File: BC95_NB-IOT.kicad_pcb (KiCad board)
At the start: 4 copper layers, 99.1 x 80 mm, 162 parts, among them J1 VIN, J2 SWD, J3 USB_B_Micro, J4 ANALOG_IN, J5 SIM_Card_Shielded, J6 INPUT, J7 OUTPUT, J8 EMPTY_PIN, Q1 2N7002, Q10 Si2301CDS, Q11 2N7002, Q12 2N7002, Q13 2N7002, Q2 2N7002, Q3 Si2301CDS, Q4 2N7002, Q5 2N7002, Q6 Si2301CDS, Q7 2N7002, Q8 2N7002, Q9 2N7002, SW1 RESET, U1 SHT4x, U10 FAN2558SX, U2 TPS54331DDA, U3 STM32L051K6Tx, U4 BG96, U5 TXS0108EPW, U6 TLV704xx, U7 FOD817ASD, U8 FOD817ASD, U9 LM1085-ADJ

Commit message: placement and routing
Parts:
- removed R64: 10k, Resistor_SMD:R_0603_1608Metric
- added C48: 100nF, Capacitor_SMD:C_0603_1608Metric, F.Cu at (75.4, 57.1)
- added C49: 100nF, Capacitor_SMD:C_0603_1608Metric, F.Cu at (70.9, 57.1)
- added D10: SMAJ28CA, Diode_SMD:D_SMA, F.Cu at (50.8, 81.0)
- added D11: SMAJ28CA, Diode_SMD:D_SMA, F.Cu at (127.4, 50.5)
- added D12: SMAJ28CA, Diode_SMD:D_SMA, F.Cu at (122.5, 50.5)
- added D13: SMAJ28CA, Diode_SMD:D_SMA, F.Cu at (99.2, 50.9)
- added D14: SMAJ28CA, Diode_SMD:D_SMA, F.Cu at (94.4, 50.8)
- added D15: SMAJ28CA, Diode_SMD:D_SMA, F.Cu at (70.6, 50.8)
- added D16: SMAJ28CA, Diode_SMD:D_SMA, F.Cu at (66.0, 50.8)
- added D17: ESDA6V1-5SC6, Package_TO_SOT_SMD:SOT-23-6, F.Cu at (133.9, 63.6)
- added R66: 470, Resistor_SMD:R_0603_1608Metric, F.Cu at (98.3, 59.4)
- added REF**: OSHW-Logo2_7.3x6mm_SilkScreen, Symbol:OSHW-Logo2_7.3x6mm_SilkScreen, F.Cu at (134.9, 53.1)
- added REF**: KiCad-Logo2_5mm_SilkScreen, Symbol:KiCad-Logo2_5mm_SilkScreen, F.Cu at (133.3, 96.5)
- added REF**: ESD-Logo_13.2x12mm_SilkScreen, Symbol:ESD-Logo_13.2x12mm_SilkScreen, F.Cu at (67.3, 103.4)
- AE1, AE2: footprint Connector_Coaxial:SMA_Amphenol_901-143_Horizontal -> Connector_Coaxial:SMA_Amphenol_901-144_Vertical
- J5: footprint Connector_Card:microSIM_JAE_SF53S006VCBR2000 -> ATTEND_MICRO_SIM:ATTEND_MICRO_SIM
- moved C30 185.6 mm to (-40.9, 56.6)
- moved D7 185.6 mm to (-28.9, 54.6)
- moved D8 185.6 mm to (-25.2, 50.2)
- moved D9 185.6 mm to (-20.9, 47.3)
- moved Q12 185.6 mm to (20.3, 8.07)
- moved Q4 185.6 mm to (-7.14, 33.1)
- moved Q8 185.6 mm to (2.90, 26.7)
- moved R12 185.6 mm to (9.86, 16.0)
- moved R30 185.6 mm to (-44.9, 56.6)
- moved R33 185.6 mm to (-33.1, 44.5)
- moved R34 185.6 mm to (15.9, 2.36)
- moved R37 185.6 mm to (26.7, -3.93)
- moved R42 185.6 mm to (0.17, 20.7)
- moved R45 185.6 mm to (-2.17, 18.2)
- moved R46 185.6 mm to (7.80, 5.96)
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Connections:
- net Net-(R10-Pad2) renamed ANALOG_IN1
- net Net-(R15-Pad1) renamed ANALOG_IN2
- D2 pad 5: unconnected-(D2-Pad5) -> +3V3
- D5 pad 5: /USB_D+ -> unconnected-(D5-Pad5)
- D5 pad 6: /USB_D- -> unconnected-(D5-Pad6)
- Q13 pad 1: 1.8V_EN -> Net-(Q13-Pad1)
- R59 pad 1: 1.8V_EN -> Net-(Q13-Pad1)
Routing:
- net +24V: track 6.32 -> 130.0 mm, vias 26 -> 28
- net V_OUT1: track 0.00 -> 80.8 mm, vias 0 -> 2
- net +3V8: track 55.0 -> 112.0 mm, vias 11 -> 58
- net +3V3: track 62.8 -> 115.4 mm, vias 2 -> 5
- net V_OUT2: track 0.00 -> 48.2 mm, vias 0 -> 2
- net V_IN2: track 0.00 -> 45.8 mm, vias 0 -> 2
- net MODULE_UART_TX: track 0.00 -> 45.1 mm, vias 0 -> 2
- net 1.8V_MONITOR: track 0.00 -> 45.0 mm, vias 0 -> 3
- net SWCLK: track 23.3 -> 64.5 mm, vias 0 -> 2
- net Net-(J4-Pad1): track 0.00 -> 39.7 mm
- net MODULE_UART_RX: track 0.00 -> 39.1 mm, vias 0 -> 3
- net Net-(R18-Pad1): track 0.00 -> 36.4 mm, vias 0 -> 2
- net V_IN1: track 0.00 -> 35.1 mm, vias 0 -> 2
- net LLC_EN: track 0.00 -> 34.0 mm, vias 0 -> 2
- net /SIM_DATA: track 0.00 -> 32.5 mm, vias 0 -> 2
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- added copper zone on F.Cu, net +6V
- added copper zone on In2.Cu, net +6V
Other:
- board size 99.1 x 80 mm -> 118.3 x 80 mm

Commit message: routing
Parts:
- removed REF**: OSHW-Logo2_7.3x6mm_SilkScreen, Symbol:OSHW-Logo2_7.3x6mm_SilkScreen
- removed REF**: KiCad-Logo2_5mm_SilkScreen, Symbol:KiCad-Logo2_5mm_SilkScreen
- removed REF**: ESD-Logo_13.2x12mm_SilkScreen, Symbol:ESD-Logo_13.2x12mm_SilkScreen
- Q11, Q12, Q4, Q5, Q8, Q9: value 2N7002 -> FDV303N
- moved R30 178.6 mm to (130.8, 88.1), turned to 90 degrees
- moved R49 176.0 mm to (132.3, 98.3)
- moved R33 166.6 mm to (132.3, 63.6), turned to -90 degrees
- moved D8 166.0 mm to (135.6, 91.4)
- moved D9 164.7 mm to (135.6, 98.3)
- moved D7 163.9 mm to (134.6, 66.3)
- moved R44 153.7 mm to (132.6, 95.1), turned to -90 degrees
- moved Q9 152.1 mm to (135.3, 59.3), turned to 0 degrees
- moved R42 150.3 mm to (130.8, 95.0), turned to 90 degrees
- moved Q8 149.1 mm to (135.4, 95.0), turned to 0 degrees
- moved R13 149.0 mm to (119.2, 63.3), turned to 0 degrees
- moved R38 147.5 mm to (132.6, 91.4)
- moved Q4 145.8 mm to (135.4, 63.6), turned to 0 degrees
- moved R34 144.9 mm to (132.6, 88.1), turned to -90 degrees
- moved Q5 143.7 mm to (135.4, 88.1), turned to 0 degrees
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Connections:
- C35 pad 1: 1.8V_MONITOR -> +1V8
- C45 pad 1: 1.8V_MONITOR -> +1V8
- C46 pad 1: 1.8V_MONITOR -> +1V8
- R61 pad 1: 1.8V_MONITOR -> +1V8
- U10 pad 6: 1.8V_MONITOR -> +1V8
- U5 pad 2: 1.8V_MONITOR -> +1V8
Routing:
- net MODULE_RST: track 0.00 -> 77.1 mm, vias 0 -> 2
- net AIRPLANE_MODE: track 0.00 -> 74.3 mm, vias 0 -> 2
- net MODULE_ON: track 0.00 -> 52.3 mm, vias 0 -> 2
- net PWR_EN: track 2.14 -> 52.2 mm, vias 1 -> 3
- net +1V8: track 0.00 -> 46.9 mm, vias 0 -> 3
- net 1.8V_MONITOR: track 45.0 -> 0.00 mm, vias 3 -> 0
- net +3V8: track 112.0 -> 156.0 mm, vias 58 -> 66
- net RESET: track 0.00 -> 35.3 mm, vias 0 -> 2
- net STATUS: track 0.00 -> 34.1 mm, vias 0 -> 2
- net NETLIGHT: track 0.00 -> 33.0 mm, vias 0 -> 2
- net PSM_IND: track 0.00 -> 31.6 mm, vias 0 -> 2
- net MODULE_UART_RX: track 39.1 -> 62.0 mm, vias 3 -> 4
- net W_DISABLE: track 0.00 -> 22.6 mm
- net PWRKEY: track 0.00 -> 18.8 mm
- net MODULE_UART_TX: track 45.1 -> 63.2 mm, vias 2 -> 3
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
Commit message: routing
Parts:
- C20, C22, C23, C25, D5, J5, R11, R14, R17, R18, R65: moved to B.Cu
- moved J5 23.2 mm to (96.5, 88.1), turned to 180 degrees
- moved D5 23.0 mm to (73.1, 101.9), turned to 180 degrees
- moved C22 19.0 mm to (88.8, 89.4), turned to 90 degrees
- moved R65 16.3 mm to (73.1, 96.2)
- moved C25 16.0 mm to (73.1, 94.2), turned to 180 degrees
- moved C20 15.1 mm to (82.4, 89.5), turned to 90 degrees
- moved C23 14.6 mm to (85.5, 89.4), turned to 90 degrees
- moved R11 8.91 mm to (90.6, 89.4)
- moved R18 8.74 mm to (92.3, 89.4)
- moved Q12 6.25 mm to (97.6, 84.9), turned to 0 degrees
- moved R57 4.82 mm to (93.0, 84.8), turned to 90 degrees
- moved R58 4.27 mm to (94.7, 84.9), turned to -90 degrees
- moved R14 3.79 mm to (83.9, 89.6)
- moved AE2 2.80 mm to (103.1, 106.6)
- moved C4 2.80 mm to (106.3, 100.1)
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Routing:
- net GND: track 0.00 -> 112.2 mm, vias 0 -> 214
- net Net-(D2-Pad1): track 3.56 -> 35.0 mm, vias 0 -> 1
- net Net-(C25-Pad1): track 36.5 -> 59.4 mm, vias 2 -> 1
- net +3V3: track 117.1 -> 138.9 mm, vias 5 -> 6
- net /SIM_RST: track 32.2 -> 19.3 mm, vias 2 -> 0
- net MODULE_RST: track 77.1 -> 67.0 mm
- net Net-(D14-Pad2): track 17.3 -> 27.2 mm, vias 0 -> 1
- net Net-(R11-Pad2): track 25.7 -> 16.7 mm, vias 2 -> 1
- net /SIM_DATA: track 32.5 -> 27.3 mm
- net ANT_GNSS: track 16.8 -> 12.1 mm
- net Net-(R14-Pad2): track 19.6 -> 23.7 mm, vias 0 -> 1
- net +6V: track 43.8 -> 40.4 mm
- net RESET: track 35.3 -> 32.2 mm
- net /SIM_CLK: track 30.5 -> 28.5 mm
- net +24V: track 132.2 -> 130.3 mm
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- added copper zone on In1.Cu, net +24V
- added copper zone on In1.Cu, net +3V8
- added copper zone on In1.Cu, net +6V
- added copper zone on F.Cu, net GND
- added copper zone on In2.Cu, net GND
- added copper zone on In1.Cu, net Net-(C17-Pad2)
- added copper zone on In1.Cu, net Net-(C39-Pad1)
- added copper zone on In1.Cu, net Net-(D1-Pad2)
- added copper zone on In1.Cu, net Net-(D10-Pad2)
- removed copper zone on In2.Cu, net +24V
- removed copper zone on In2.Cu, net +3V8
- removed copper zone on In2.Cu, net +6V
- removed copper zone on In2.Cu, net Net-(C17-Pad2)
- removed copper zone on In2.Cu, net Net-(C39-Pad1)
- removed copper zone on In2.Cu, net Net-(D1-Pad2)
- removed copper zone on In2.Cu, net Net-(D10-Pad2)

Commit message: board layout
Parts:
- added R64: 10k, Resistor_SMD:R_0603_1608Metric, F.Cu at (77.1, 57.1)
- added REF**: hyc, HYC:hyc, F.Cu at (73.9, 67.7)
- U4: value BG96 -> QUECTEL_BG96
- moved C1 2.58 mm to (80.1, 71.0), turned to 180 degrees
- moved R50 2.04 mm to (66.3, 84.7)
- moved R52 1.78 mm to (64.5, 84.7)
- moved C48 0.15 mm to (75.3, 57.1)
- moved U4 0.06 mm to (115.0, 80.7)
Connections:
- U3 pad 9: 1.8V_MONITOR -> +1V8
- U4 pad 12: unconnected-(U4-Pad11) -> unconnected-(U4-Pad12)
- U4 pad 13: unconnected-(U4-Pad11) -> unconnected-(U4-Pad13)
- U4 pad 14: unconnected-(U4-Pad11) -> unconnected-(U4-Pad14)
- U4 pad 16: unconnected-(U4-Pad11) -> unconnected-(U4-Pad16)
- U4 pad 25: unconnected-(U4-Pad11) -> unconnected-(U4-Pad25)
- U4 pad 51: unconnected-(U4-Pad11) -> unconnected-(U4-Pad51)
- U4 pad 56: unconnected-(U4-Pad11) -> unconnected-(U4-Pad56)
- U4 pad 57: unconnected-(U4-Pad11) -> unconnected-(U4-Pad57)
- U4 pad 63: unconnected-(U4-Pad11) -> unconnected-(U4-Pad63)
- U4 pad 65: unconnected-(U4-Pad11) -> unconnected-(U4-Pad65)
- U4 pad 66: unconnected-(U4-Pad11) -> unconnected-(U4-Pad66)
- U4 pad 76: unconnected-(U4-Pad11) -> unconnected-(U4-Pad76)
- U4 pad 77: unconnected-(U4-Pad11) -> unconnected-(U4-Pad77)
- U4 pad 78: unconnected-(U4-Pad11) -> unconnected-(U4-Pad78)
- U4 pad 83: unconnected-(U4-Pad11) -> unconnected-(U4-Pad83)
- U4 pad 84: unconnected-(U4-Pad11) -> unconnected-(U4-Pad84)
- U4 pad 85: unconnected-(U4-Pad11) -> unconnected-(U4-Pad85)
- U4 pad 86: unconnected-(U4-Pad11) -> unconnected-(U4-Pad86)
- U4 pad 87: unconnected-(U4-Pad11) -> unconnected-(U4-Pad87)
- U4 pad 88: unconnected-(U4-Pad11) -> unconnected-(U4-Pad88)
- U4 pad 92: unconnected-(U4-Pad11) -> unconnected-(U4-Pad92)
- U4 pad 93: unconnected-(U4-Pad11) -> unconnected-(U4-Pad93)
- U4 pad 94: unconnected-(U4-Pad11) -> unconnected-(U4-Pad94)
- U4 pad 95: unconnected-(U4-Pad11) -> unconnected-(U4-Pad95)
- U4 pad 96: unconnected-(U4-Pad11) -> unconnected-(U4-Pad96)
- U4 pad 97: unconnected-(U4-Pad11) -> unconnected-(U4-Pad97)
- U4 pad 98: unconnected-(U4-Pad11) -> unconnected-(U4-Pad98)
- U4 pad 99: unconnected-(U4-Pad11) -> unconnected-(U4-Pad99)
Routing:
- net SWDIO: track 31.5 -> 45.8 mm, vias 0 -> 2
- net GND: track 112.2 -> 120.2 mm, vias 214 -> 588
- net NRST: track 9.45 -> 11.4 mm
- net +3V8: track 156.0 -> 157.9 mm
- net +1V8: track 46.9 -> 48.0 mm
- net /SIM_RST: track 19.3 -> 20.3 mm
- net LLC_EN: track 33.8 -> 32.9 mm
- net Net-(R7-Pad2): track 43.8 -> 42.9 mm
- net V_IN2: track 48.4 -> 49.2 mm
- net Net-(R6-Pad2): track 42.5 -> 41.8 mm
- net +3V3: track 138.9 -> 138.2 mm
- net Net-(C25-Pad1): track 59.4 -> 60.0 mm
- net (no net): vias 1 -> 0
- added copper zone on B.Cu, net GND

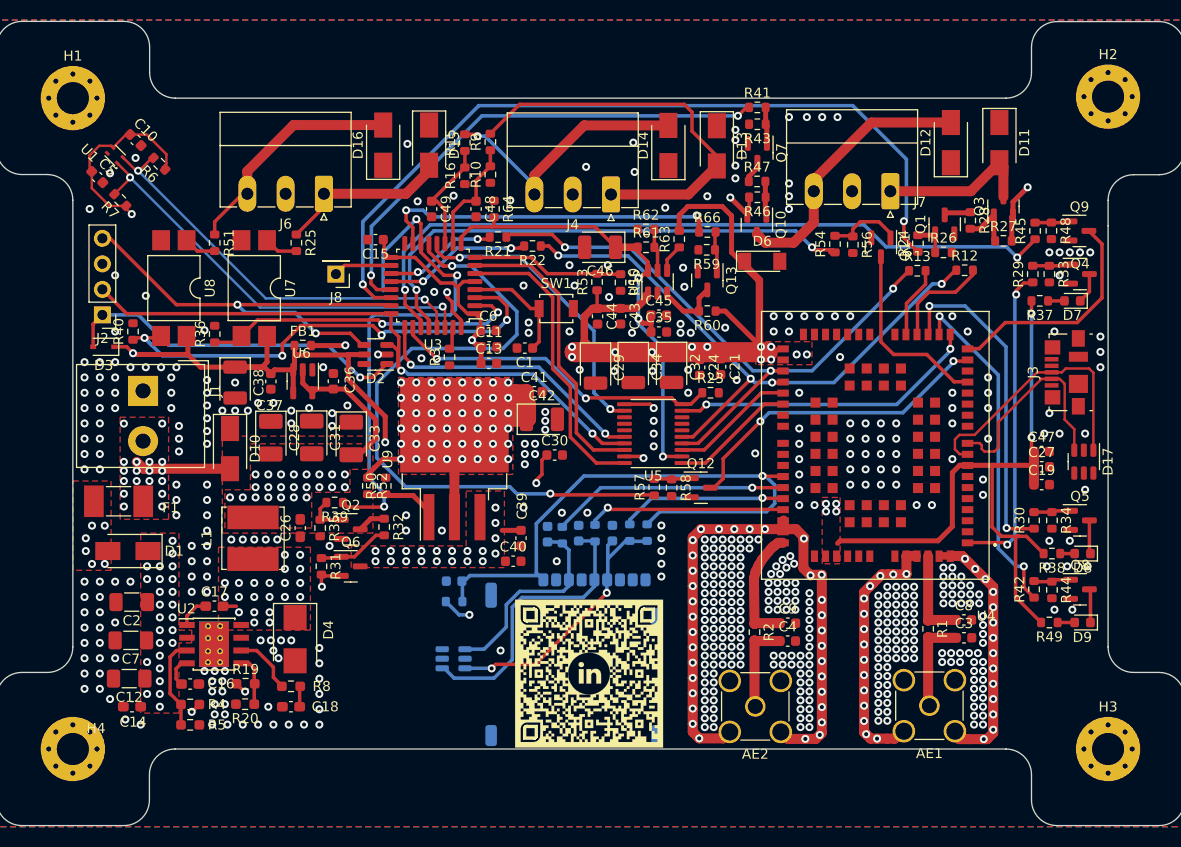
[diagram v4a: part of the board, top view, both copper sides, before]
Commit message: 3d models added.
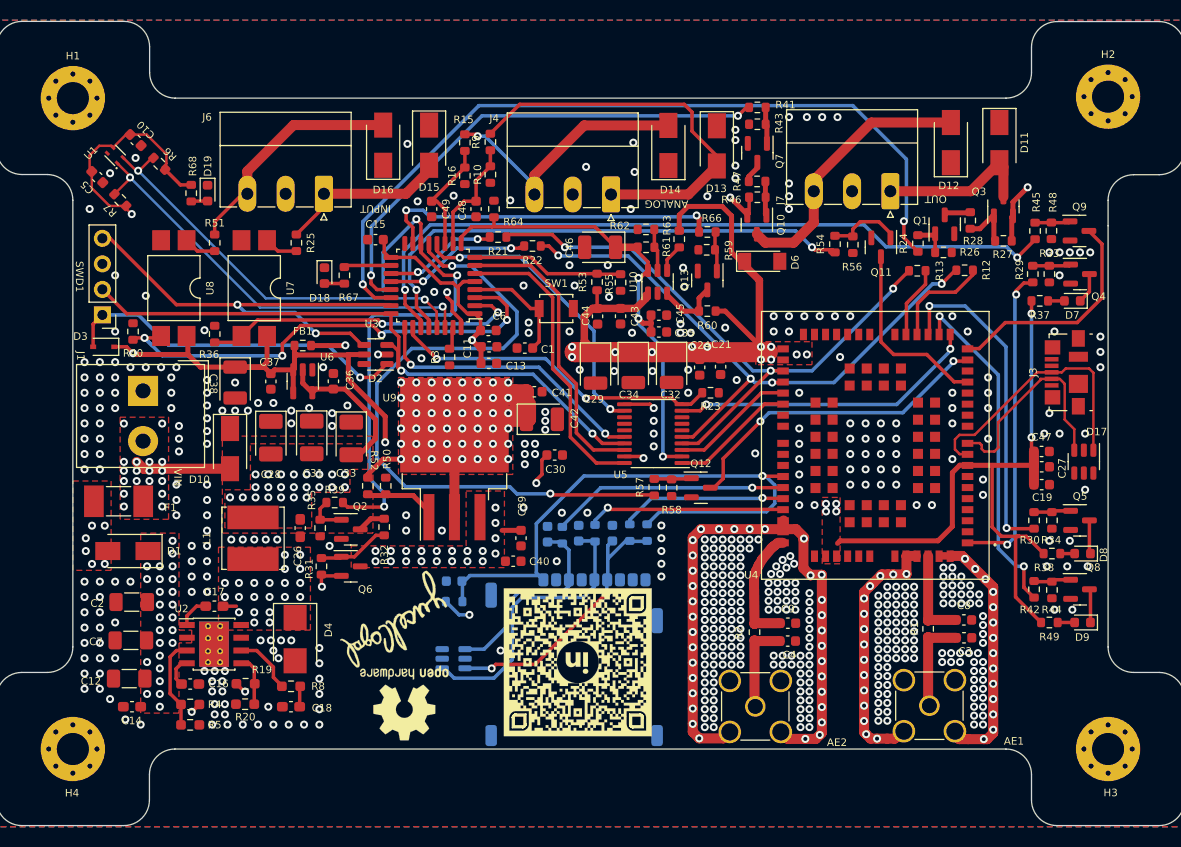
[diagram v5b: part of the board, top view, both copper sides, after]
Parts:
- removed J8: EMPTY_PIN, Connector_PinHeader_2.54mm:PinHeader_1x01_P2.54mm_Vertical
- added D18: LED, LED_SMD:LED_0603_1608Metric, F.Cu at (60.2, 63.8)
- added D19: LED, LED_SMD:LED_0603_1608Metric, F.Cu at (48.6, 55.6)
- added R67: 510, Resistor_SMD:R_0603_1608Metric, F.Cu at (62.2, 63.8)
- added R68: 510, Resistor_SMD:R_0603_1608Metric, F.Cu at (46.9, 55.6)
- added REF**: sign, HYC:sign, F.Cu at (74.0, 98.8)
- added REF**: OSHW-Logo2_9.8x8mm_SilkScreen, Symbol:OSHW-Logo2_9.8x8mm_SilkScreen, F.Cu at (68.1, 106.3)
- REF**: value hyc -> LinkedIn
- moved REF** 25.2 mm to (76.6, 92.7)
- renumbered J2 to SWD1
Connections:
- U3 pad 18: Net-(J8-Pad1) -> TOGGLE_LED
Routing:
- net Net-(J8-Pad1): track 5.83 -> 0.00 mm
- net TOGGLE_LED: track 0.00 -> 4.62 mm
- net +3V3: track 138.2 -> 141.4 mm
- net Net-(D18-Pad2): track 0.00 -> 1.99 mm
- net Net-(D19-Pad2): track 0.00 -> 1.64 mm
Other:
- board text added: "ANALOG"
- board text added: "INPUT"
- board text added: "OUT"
- board text added: "VIN"
